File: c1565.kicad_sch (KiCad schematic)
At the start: 6 parts, among them J4 Mini-DIN-8-With-Shield, U12 74LS125, U13 74LS125

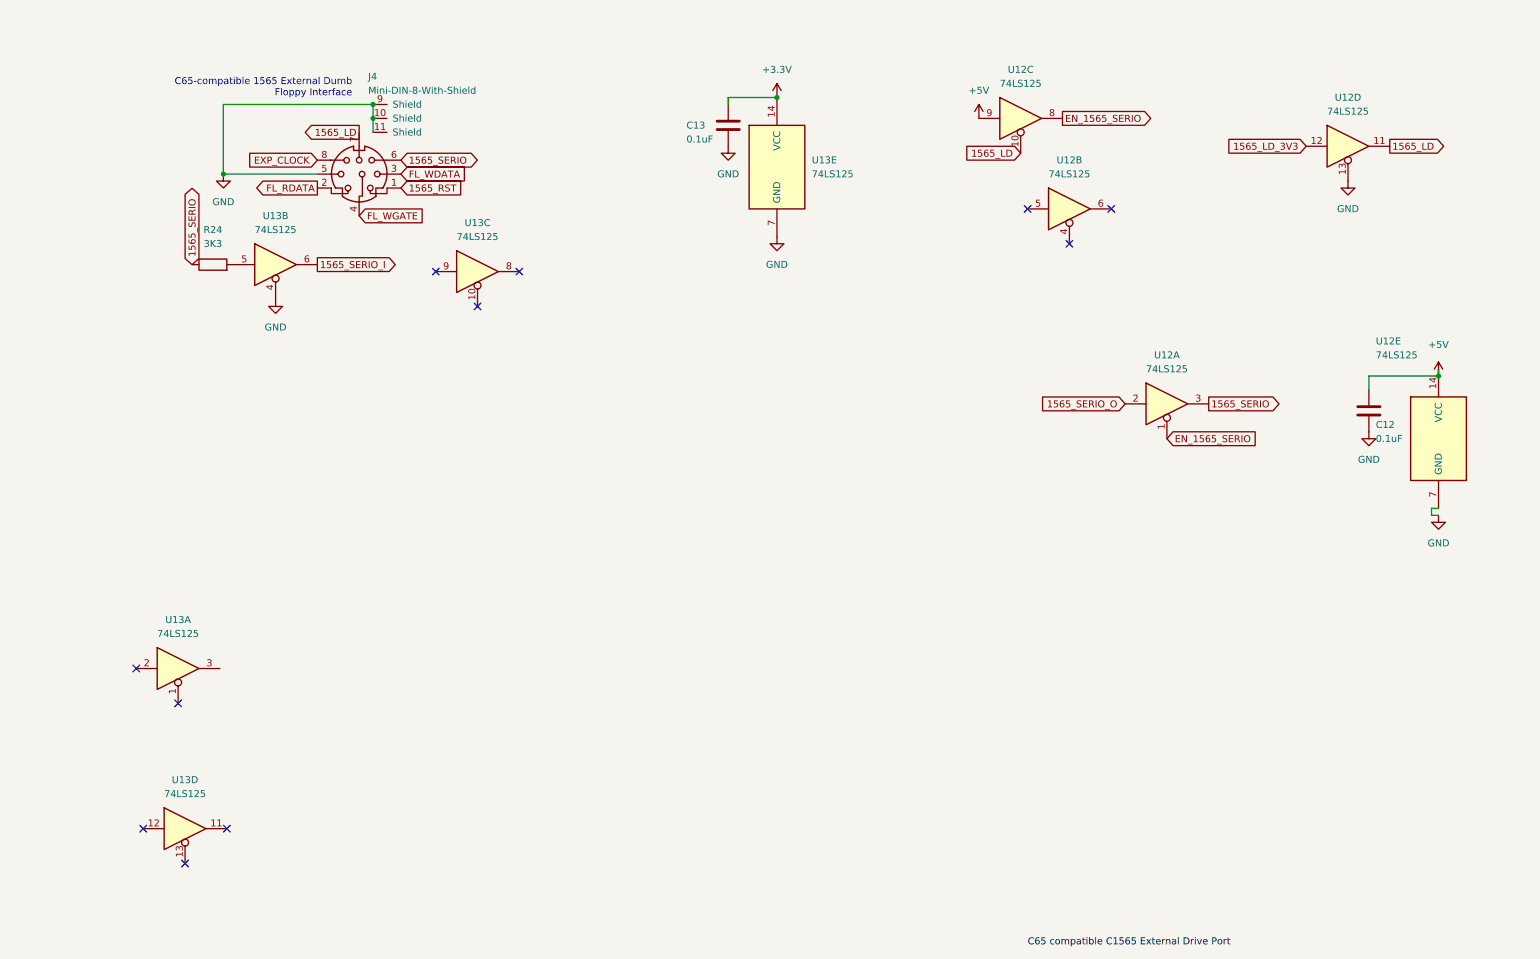
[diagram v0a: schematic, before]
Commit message: tidy up C1565 port schematic and plumbing
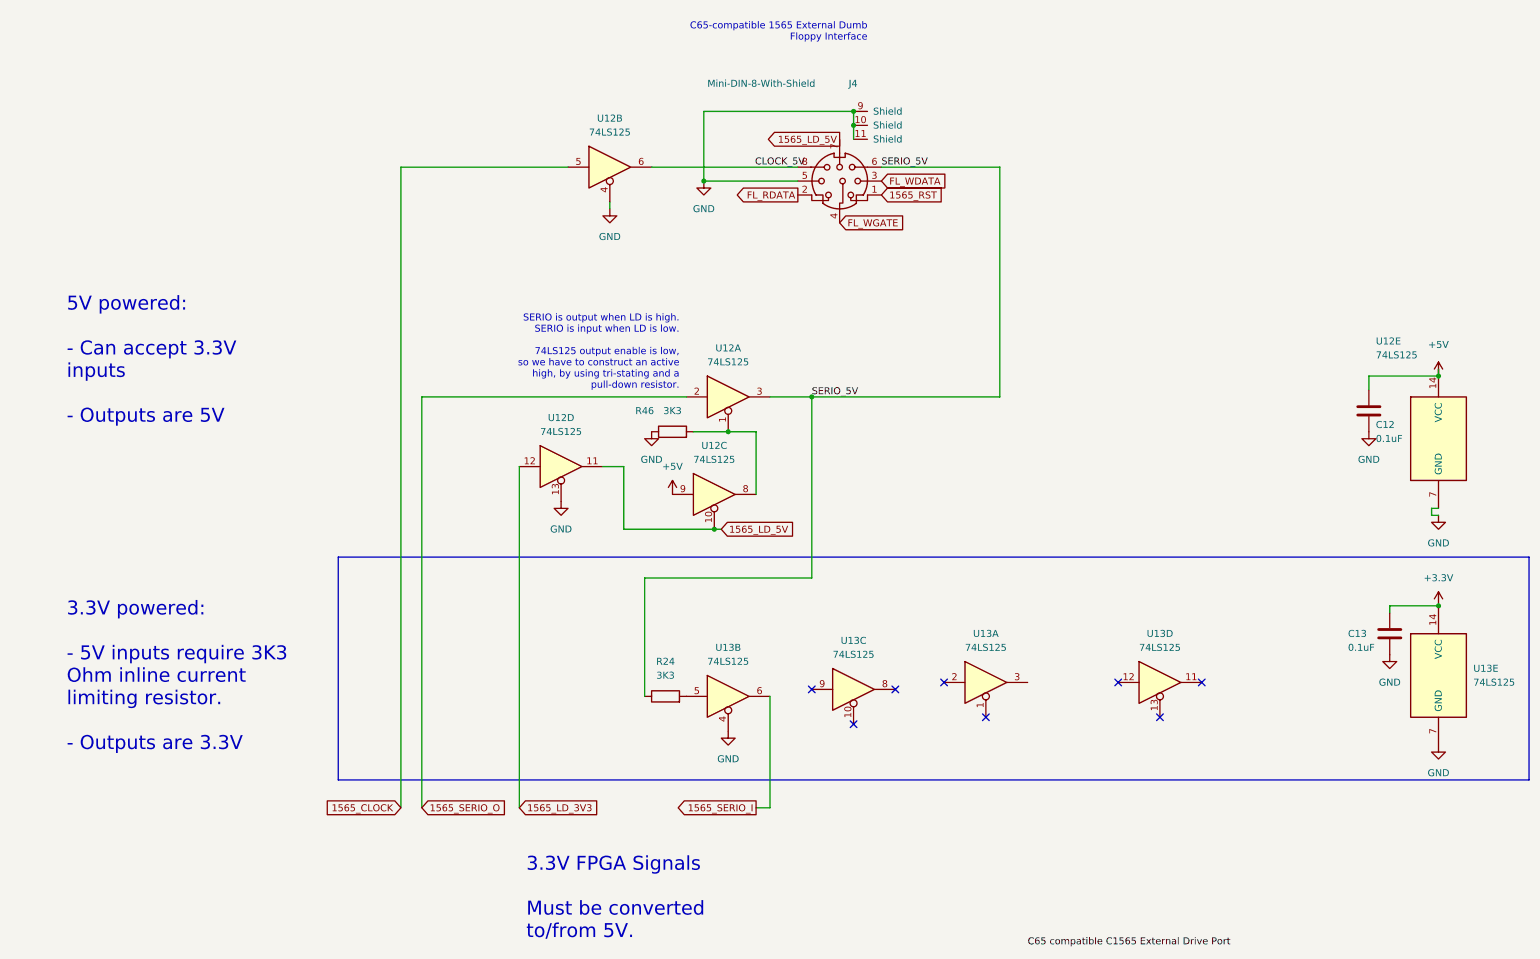
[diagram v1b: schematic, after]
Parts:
- added R46: 3K3, snapeda:Labeled Resistor, symbol Device:R
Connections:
- net EXP_CLOCK is gone; now on an unnamed net: J4.8
- net GND: now also U12.4, R46.1
- net 1565_CLOCK: now reaches U12.5
- net 1565_LD renamed 1565_LD_5V
- net 1565_SERIO renamed SERIO_5V
- net EN_1565_SERIO: no longer names the net of U12.1, U12.8
- net EN_1565_SERIO: now also R46.2
- no-connect marks 11 -> 8
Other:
- note added: "3.3V FPGA Signals Must be converted to/from 5V."
- note added: "3.3V powered: - 5V inputs require 3K3 Ohm inline current limiting resistor. - Outputs are 3.3V"
- note added: "5V powered: - Can accept 3.3V inputs - Outputs are 5V"
- note added: "SERIO is output when LD is high. SERIO is input when LD is low. 74LS125 output enable is low, so we have to construct an active high, by using tri-stating and a pull-down resistor."
- moved on the sheet: C13, J4, R24, U12A, U12B, U12C, U12D, U13A, U13B, U13C, U13D, U13E

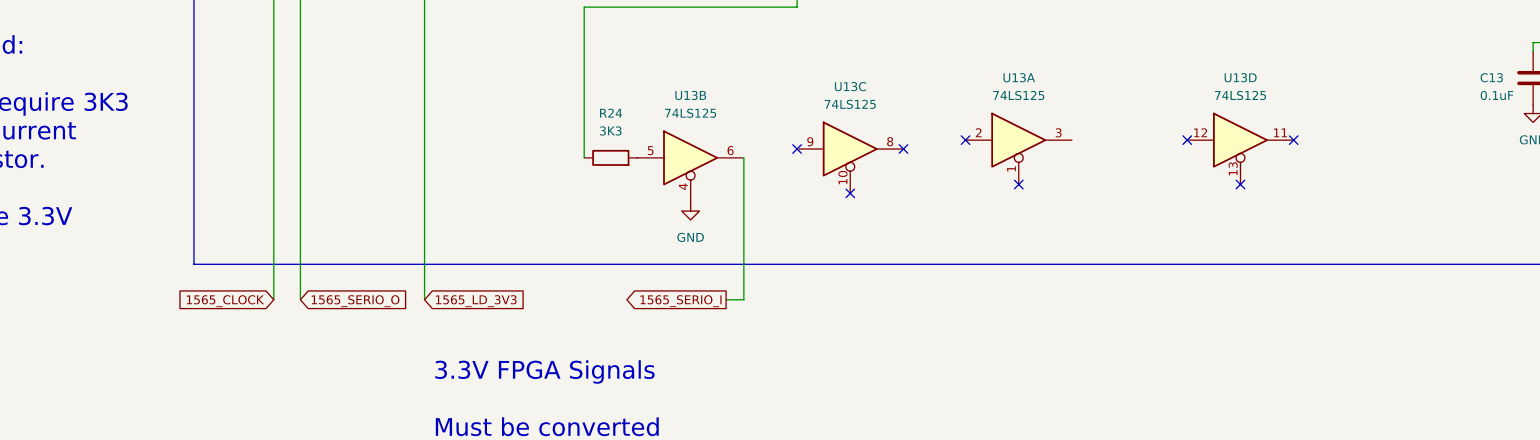
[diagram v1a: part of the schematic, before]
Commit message: reroute 1565 clock, LD and 5V WIFI_EN line
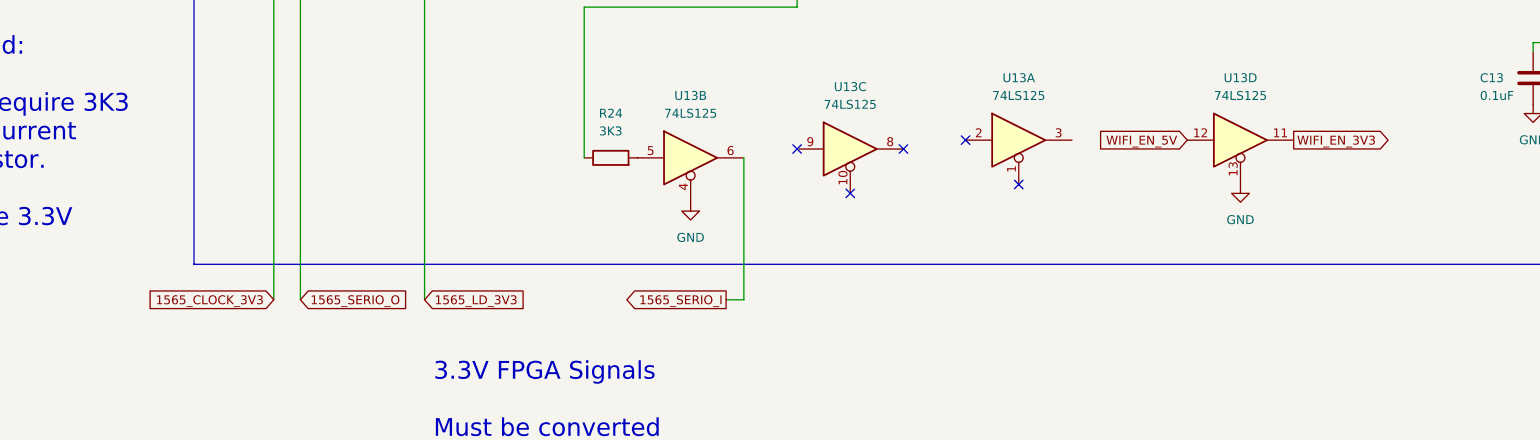
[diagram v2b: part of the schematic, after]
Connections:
- net GND: now also U13.13
- net WIFI_EN_3V3: now reaches U13.11
- net WIFI_EN_5V: now reaches U13.12
- net 1565_CLOCK renamed 1565_CLOCK_3V3
- no-connect marks 8 -> 5
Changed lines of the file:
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@@
   )
   (no_connect (at 182.88 148.59))
-  (no_connect (at 222.25 142.24))
   (no_connect (at 151.13 143.51))
   (no_connect (at 175.26 142.24))
   (no_connect (at 158.75 149.86))
-  (no_connect (at 214.63 148.59))
   (no_connect (at 166.37 143.51))
-  (no_connect (at 207.01 142.24))
   (wire (pts (xy 264.16 110.49) (xy 264.16 111.76))
     (stroke (width 0) (type default))
@@
     )
   )
-  (global_label "1565_CLOCK" (shape input) (at 76.2 165.1 180) (fields_autoplaced)
+  (global_label "1565_CLOCK_3V3" (shape input) (at 76.2 165.1 180) (fields_autoplaced)
     (effects (font (size 1.27 1.27)) (justify right))
-    (property "Intersheetrefs" "${INTERSHEET_REFS}" (at 61.8948 165.1 0)
+    (property "Intersheetrefs" "${INTERSHEET_REFS}" (at 57.4196 165.1 0)
       (effects (font (size 1.27 1.27)) (justify right) hide)
+    )
+  )
+  (global_label "WIFI_EN_3V3" (shape output) (at 222.25 142.24 0) (fields_autoplaced)
+    (effects (font (size 1.27 1.27)) (justify left))
+    (property "Intersheetrefs" "${INTERSHEET_REFS}" (at 236.2529 142.24 0)
+      (effects (font (size 1.27 1.27)) (justify left) hide)
     )
   )
@@
     (property "Intersheetrefs" "${INTERSHEET_REFS}" (at 167.5452 58.3406 0)
       (effects (font (size 1.27 1.27)) (justify left) hide)
+    )
+  )
+  (global_label "WIFI_EN_5V" (shape input) (at 207.01 142.24 180) (fields_autoplaced)
+    (effects (font (size 1.27 1.27)) (justify right))
+    (property "Intersheetrefs" "${INTERSHEET_REFS}" (at 194.2166 142.24 0)
+      (effects (font (size 1.27 1.27)) (justify right) hide)
     )
   )
@@
         )
       )
+    )
+  )
+  (symbol (lib_name "GND_5") (lib_id "power:GND") (at 214.63 148.59 0) (unit 1)
+    (in_bom yes) (on_board yes) (dnp no) (fields_autoplaced)
+    (property "Reference" "#PWR0111" (at 214.63 154.94 0)
+      (effects (font (size 1.27 1.27)) hide)
+    )
+    (property "Value" "GND" (at 214.63 153.67 0)
+      (effects (font (size 1.27 1.27)))
+    )
+    (property "Footprint" "" (at 214.63 148.59 0)
+      (effects (font (size 1.27 1.27)) hide)
+    )
+    (property "Datasheet" "" (at 214.63 148.59 0)
+      (effects (font (size 1.27 1.27)) hide)
+    )
+    (pin "1")
+    (instances
+      (project "mega65-r3-expansion-board.kicad"
+        (path "/e63e39d7-6ac0-4ffd-8aa3-1841a4541b55/146a8bef-6809-4ca3-9c51-e7afef5be129"
+          (reference "#PWR0111") (unit 1)
+        )
+      )
